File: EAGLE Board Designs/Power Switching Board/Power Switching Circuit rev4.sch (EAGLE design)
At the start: 63 parts, among them J1 CONNECTOR-4_SOURIAU_, J2 CONNECTOR-3_8STA20435PN, J3 CONNECTOR-4_SOURIAU_, K1 RELAY_SOLIDSTATE_NO_CMX60D20, Q1 TRANSISTOR_N_MOS_2-7K1S_TK100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, Q2 TRANSISTOR_N_MOS_2-7K1S_TK100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, Q3 TRANSISTOR_N_MOS_2-7K1S_TK100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, Q4 TRANSISTOR_N_MOS_2-7K1S_TK100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, U1 LTC4421

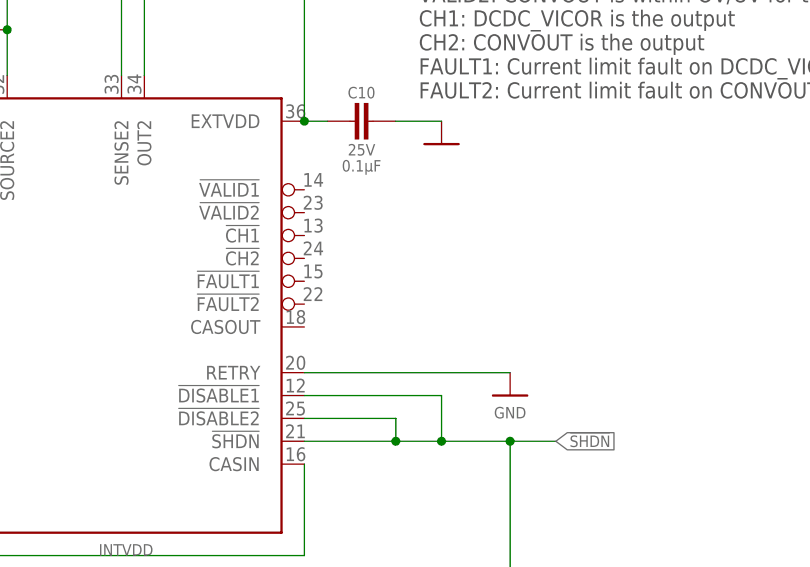
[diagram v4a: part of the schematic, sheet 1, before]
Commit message: Connected Data Out pins to GND
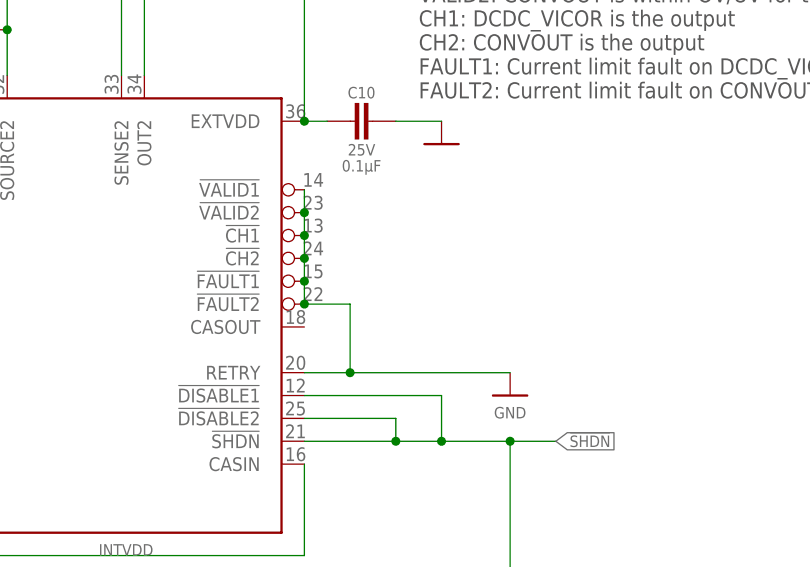
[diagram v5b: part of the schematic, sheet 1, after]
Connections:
- net GND: now also U1.!CH1, U1.!CH2, U1.!FAULT1, U1.!FAULT2, U1.!VALID1, U1.!VALID2
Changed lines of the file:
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@@
 <segment>
 <pinref part="U1" gate="G$1" pin="RETRY"/>
-<wire x1="55.88" y1="-40.64" x2="78.74" y2="-40.64" width="0.1524" layer="91"/>
+<wire x1="55.88" y1="-40.64" x2="60.96" y2="-40.64" width="0.1524" layer="91"/>
 <pinref part="P10" gate="1" pin="GND"/>
+<pinref part="U1" gate="G$1" pin="!VALID1"/>
+<pinref part="U1" gate="G$1" pin="!VALID2"/>
+<wire x1="60.96" y1="-40.64" x2="78.74" y2="-40.64" width="0.1524" layer="91"/>
+<wire x1="55.88" y1="-20.32" x2="55.88" y2="-22.86" width="0.1524" layer="91"/>
+<pinref part="U1" gate="G$1" pin="!CH1"/>
+<wire x1="55.88" y1="-22.86" x2="55.88" y2="-25.4" width="0.1524" layer="91"/>
+<junction x="55.88" y="-22.86"/>
+<pinref part="U1" gate="G$1" pin="!CH2"/>
+<wire x1="55.88" y1="-25.4" x2="55.88" y2="-27.94" width="0.1524" layer="91"/>
+<junction x="55.88" y="-25.4"/>
+<pinref part="U1" gate="G$1" pin="!FAULT1"/>
+<wire x1="55.88" y1="-27.94" x2="55.88" y2="-30.48" width="0.1524" layer="91"/>
+<junction x="55.88" y="-27.94"/>
+<pinref part="U1" gate="G$1" pin="!FAULT2"/>
+<wire x1="55.88" y1="-30.48" x2="55.88" y2="-33.02" width="0.1524" layer="91"/>
+<junction x="55.88" y="-30.48"/>
+<wire x1="55.88" y1="-33.02" x2="60.96" y2="-33.02" width="0.1524" layer="91"/>
+<wire x1="60.96" y1="-33.02" x2="60.96" y2="-40.64" width="0.1524" layer="91"/>
+<junction x="55.88" y="-33.02"/>
+<junction x="60.96" y="-40.64"/>
 </segment>
 <segment>

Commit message: Final fixes of board
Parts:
- TP3: value TEST_POINT -> INTVDD
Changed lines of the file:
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@@
 <part name="TP12" library="HyTechDevices" deviceset="TEST_POINT" device=""/>
 <part name="TP2" library="HyTechDevices" deviceset="TEST_POINT" device=""/>
-<part name="TP3" library="HyTechDevices" deviceset="TEST_POINT" device=""/>
+<part name="TP3" library="HyTechDevices" deviceset="TEST_POINT" device="" value="INTVDD"/>
 <part name="TP6" library="HyTechDevices" deviceset="TEST_POINT" device=""/>
 <part name="O1" library="HyTechExternal" deviceset="FUSE_*" device="" technology="MINI_BLADE_10"/>
